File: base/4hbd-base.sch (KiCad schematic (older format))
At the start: 13 parts, among them J1 Screw_Terminal_01x03, J10 Screw_Terminal_01x04, J11 Screw_Terminal_01x02, J12 Conn_01x03, J13 Conn_01x08, J2 Screw_Terminal_01x03, J3 Screw_Terminal_01x03, J4 Screw_Terminal_01x03, J5 Screw_Terminal_01x02, J6 Screw_Terminal_01x02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

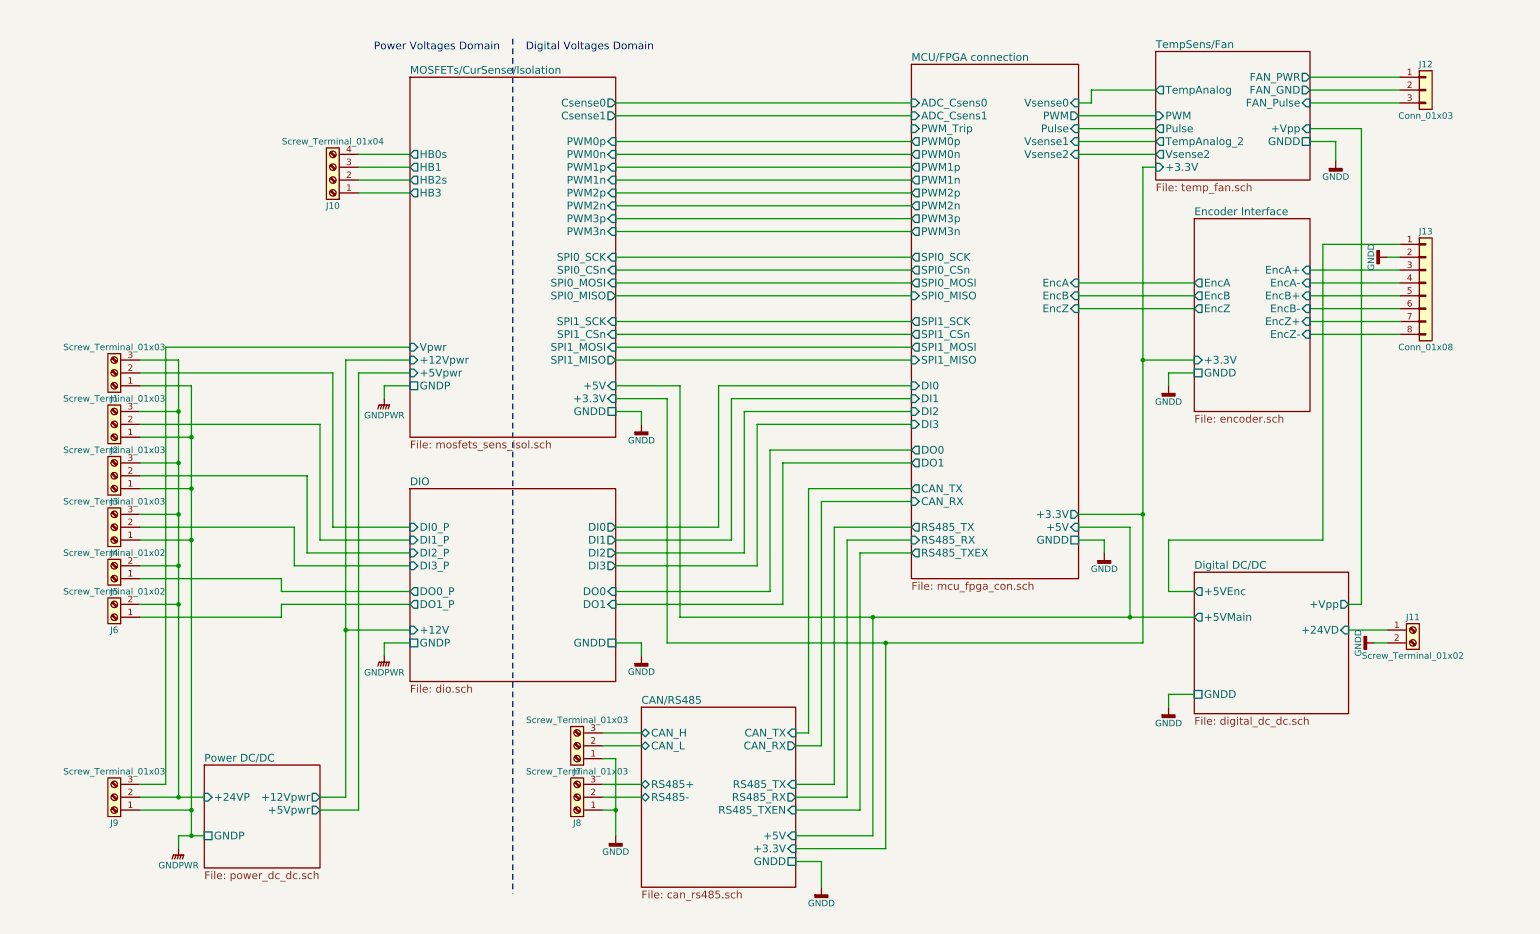
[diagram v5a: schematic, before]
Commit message: some test points
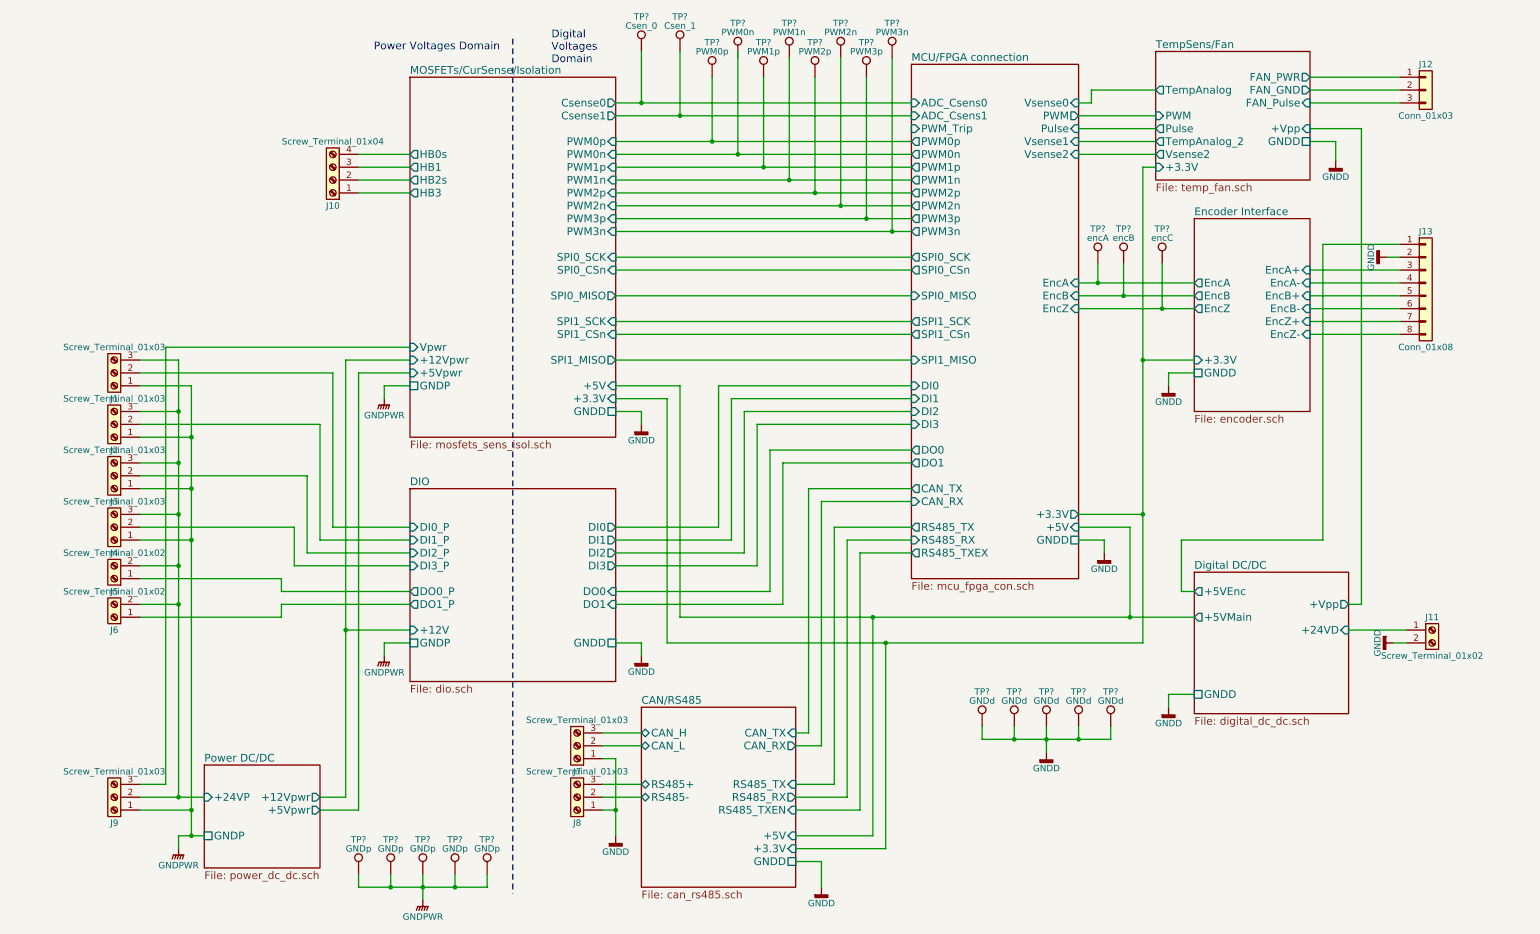
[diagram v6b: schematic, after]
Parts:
- added TP?: PWM0p, symbol Test_Point
- added TP?: PWM0n, symbol Test_Point
- added TP?: PWM1p, symbol Test_Point
- added TP?: PWM1n, symbol Test_Point
- added TP?: PWM2p, symbol Test_Point
- added TP?: PWM2n, symbol Test_Point
- added TP?: PWM3p, symbol Test_Point
- added TP?: PWM3n, symbol Test_Point
- added TP?: Csen_0, symbol Test_Point
- added TP?: Csen_1, symbol Test_Point
- added TP?: encA, symbol Test_Point
- added TP?: encB, symbol Test_Point
- added TP?: encC, symbol Test_Point
- added TP? (x5): GNDd, symbol Test_Point
- added TP? (x5): GNDp, symbol Test_Point
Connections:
- net Encoder Interface/EncA: now also TP?.1
- net Encoder Interface/EncB: now also TP?.1
- net Encoder Interface/EncZ: now also TP?.1
- net GNDD: now also TP?.1, TP?.1, TP?.1, TP?.1, TP?.1
- net GNDPWR: now also TP?.1, TP?.1, TP?.1, TP?.1, TP?.1
- net MCU/FPGA connection/ADC_Csens0: now also TP?.1
- net MCU/FPGA connection/ADC_Csens1: now also TP?.1
- net MCU/FPGA connection/PWM0p: now also TP?.1
- net MCU/FPGA connection/PWM1n: now also TP?.1
- net MCU/FPGA connection/PWM1p: now also TP?.1
- net MCU/FPGA connection/PWM2n: now also TP?.1
- net MCU/FPGA connection/PWM2p: now also TP?.1
- net MCU/FPGA connection/PWM3n: now also TP?.1
- net MCU/FPGA connection/PWM3p: now also TP?.1
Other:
- note added: "Digital \nVoltages\nDomain"
- note removed: "Digital Voltages Domain"
- moved on the sheet: J11

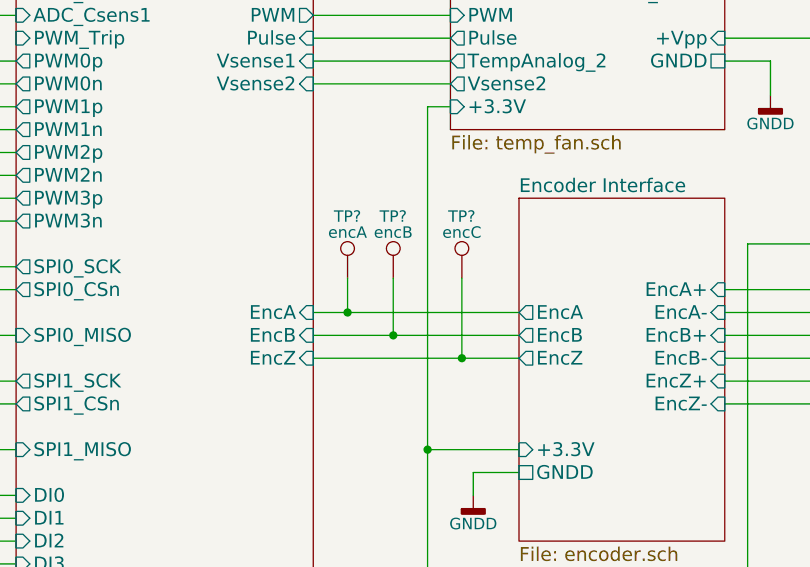
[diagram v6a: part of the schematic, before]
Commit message: A few updates to test points.
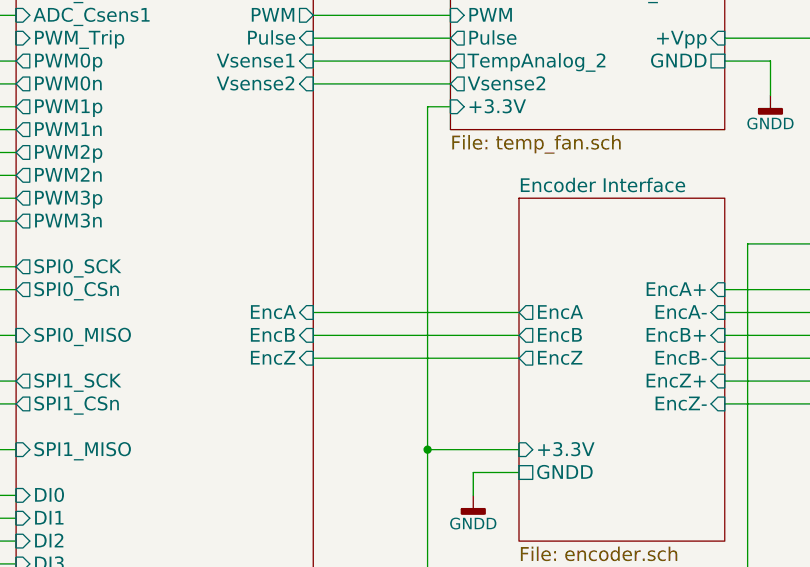
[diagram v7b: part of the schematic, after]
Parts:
- removed TP?: encA, symbol Test_Point
- removed TP?: encB, symbol Test_Point
- removed TP?: encC, symbol Test_Point
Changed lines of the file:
@@
 F14 "SPI0_SCK" I R 4600 2500 60
 F15 "SPI0_CSn" I R 4600 2600 60
-F17 "SPI0_MISO" O R 4600 2800 60
-F18 "SPI1_SCK" I R 4600 3000 60
-F19 "SPI1_CSn" I R 4600 3100 60
-F21 "SPI1_MISO" O R 4600 3300 60
-F22 "+3.3V" I R 4600 3600 60
-F23 "GNDD" U R 4600 3700 60
-F24 "Vpwr" I L 3000 3200 60
-F25 "+12Vpwr" I L 3000 3300 60
-F26 "GNDP" U L 3000 3500 60
-F27 "+5Vpwr" I L 3000 3400 60
-F28 "+5V" I R 4600 3500 60
-F29 "Csense0" O R 4600 1300 60
-F30 "Csense1" O R 4600 1400 60
+F16 "SPI0_MISO" O R 4600 2800 60
+F17 "SPI1_SCK" I R 4600 3000 60
+F18 "SPI1_CSn" I R 4600 3100 60
+F19 "SPI1_MISO" O R 4600 3300 60
+F20 "+3.3V" I R 4600 3600 60
+F21 "GNDD" U R 4600 3700 60
+F22 "Vpwr" I L 3000 3200 60
+F23 "+12Vpwr" I L 3000 3300 60
+F24 "GNDP" U L 3000 3500 60
+F25 "+5Vpwr" I L 3000 3400 60
+F26 "+5V" I R 4600 3500 60
+F27 "Csense0" O R 4600 1300 60
+F28 "Csense1" O R 4600 1400 60
 $EndSheet
 $Sheet
@@
 F10 "SPI0_SCK" O L 6900 2500 60
 F11 "SPI0_CSn" O L 6900 2600 60
-F13 "SPI0_MISO" I L 6900 2800 60
-F14 "SPI1_SCK" O L 6900 3000 60
-F15 "SPI1_CSn" O L 6900 3100 60
-F17 "SPI1_MISO" I L 6900 3300 60
-F18 "DI0" I L 6900 3500 60
-F19 "DI1" I L 6900 3600 60
-F20 "DI2" I L 6900 3700 60
-F21 "DI3" I L 6900 3800 60
-F22 "DO0" O L 6900 4000 60
-F23 "DO1" O L 6900 4100 60
-F24 "CAN_TX" O L 6900 4300 60
-F25 "CAN_RX" I L 6900 4400 60
-F26 "RS485_TX" O L 6900 4600 60
-F27 "RS485_RX" I L 6900 4700 60
-F28 "RS485_TXEX" O L 6900 4800 60
-F29 "+5V" I R 8200 4600 60
-F30 "GNDD" U R 8200 4700 60
-F31 "EncA" I R 8200 2700 60
-F32 "EncB" I R 8200 2800 60
-F33 "EncZ" I R 8200 2900 60
-F34 "PWM" O R 8200 1400 60
-F35 "Pulse" I R 8200 1500 60
-F36 "Vsense1" I R 8200 1600 60
-F37 "+3.3V" O R 8200 4500 60
-F38 "PWM_Trip" I L 6900 1500 60
-F39 "Vsense0" I R 8200 1300 60
-F40 "ADC_Csens1" I L 6900 1400 60
-F41 "ADC_Csens0" I L 6900 1300 60
-F42 "Vsense2" I R 8200 1700 60
+F12 "SPI0_MISO" I L 6900 2800 60
+F13 "SPI1_SCK" O L 6900 3000 60
+F14 "SPI1_CSn" O L 6900 3100 60
+F15 "SPI1_MISO" I L 6900 3300 60
+F16 "DI0" I L 6900 3500 60
+F17 "DI1" I L 6900 3600 60
+F18 "DI2" I L 6900 3700 60
+F19 "DI3" I L 6900 3800 60
+F20 "DO0" O L 6900 4000 60
+F21 "DO1" O L 6900 4100 60
+F22 "CAN_TX" O L 6900 4300 60
+F23 "CAN_RX" I L 6900 4400 60
+F24 "RS485_TX" O L 6900 4600 60
+F25 "RS485_RX" I L 6900 4700 60
+F26 "RS485_TXEX" O L 6900 4800 60
+F27 "+5V" I R 8200 4600 60
+F28 "GNDD" U R 8200 4700 60
+F29 "EncA" I R 8200 2700 60
+F30 "EncB" I R 8200 2800 60
+F31 "EncZ" I R 8200 2900 60
+F32 "PWM" O R 8200 1400 60
+F33 "Pulse" I R 8200 1500 60
+F34 "Vsense1" I R 8200 1600 60
+F35 "+3.3V" O R 8200 4500 60
+F36 "PWM_Trip" I L 6900 1500 60
+F37 "Vsense0" I R 8200 1300 60
+F38 "ADC_Csens1" I L 6900 1400 60
+F39 "ADC_Csens0" I L 6900 1300 60
+F40 "Vsense2" I R 8200 1700 60
 $EndSheet
 $Sheet
@@
 Connection ~ 5100 1400
 $Comp
-L Test_Point TP?
-U 1 1 5A478D44
-P 8350 2550
-F 0 "TP?" H 8350 2820 50  0000 C CNN
-F 1 "encA" H 8350 2750 50  0000 C CNN
-F 2 "" H 8550 2550 50  0001 C CNN
-F 3 "" H 8550 2550 50  0001 C CNN
-	1    8350 2550
-	1    0    0    -1
-$EndComp
-$Comp
-L Test_Point TP?
-U 1 1 5A479C9D
-P 8550 2550
-F 0 "TP?" H 8550 2820 50  0000 C CNN
-F 1 "encB" H 8550 2750 50  0000 C CNN
-F 2 "" H 8750 2550 50  0001 C CNN
-F 3 "" H 8750 2550 50  0001 C CNN
-	1    8550 2550
-	1    0    0    -1
-$EndComp
-$Comp
-L Test_Point TP?
-U 1 1 5A47A006
-P 8850 2550
-F 0 "TP?" H 8850 2820 50  0000 C CNN
-F 1 "encC" H 8850 2750 50  0000 C CNN
-F 2 "" H 9050 2550 50  0001 C CNN
-F 3 "" H 9050 2550 50  0001 C CNN
-	1    8850 2550
-	1    0    0    -1
-$EndComp
-Wire Wire Line
-	8350 2550 8350 2700
-Connection ~ 8350 2700
-Wire Wire Line
-	8550 2550 8550 2800
-Connection ~ 8550 2800
-Wire Wire Line
-	8850 2550 8850 2900
-Connection ~ 8850 2900
-$Comp
 L GNDD #PWR?

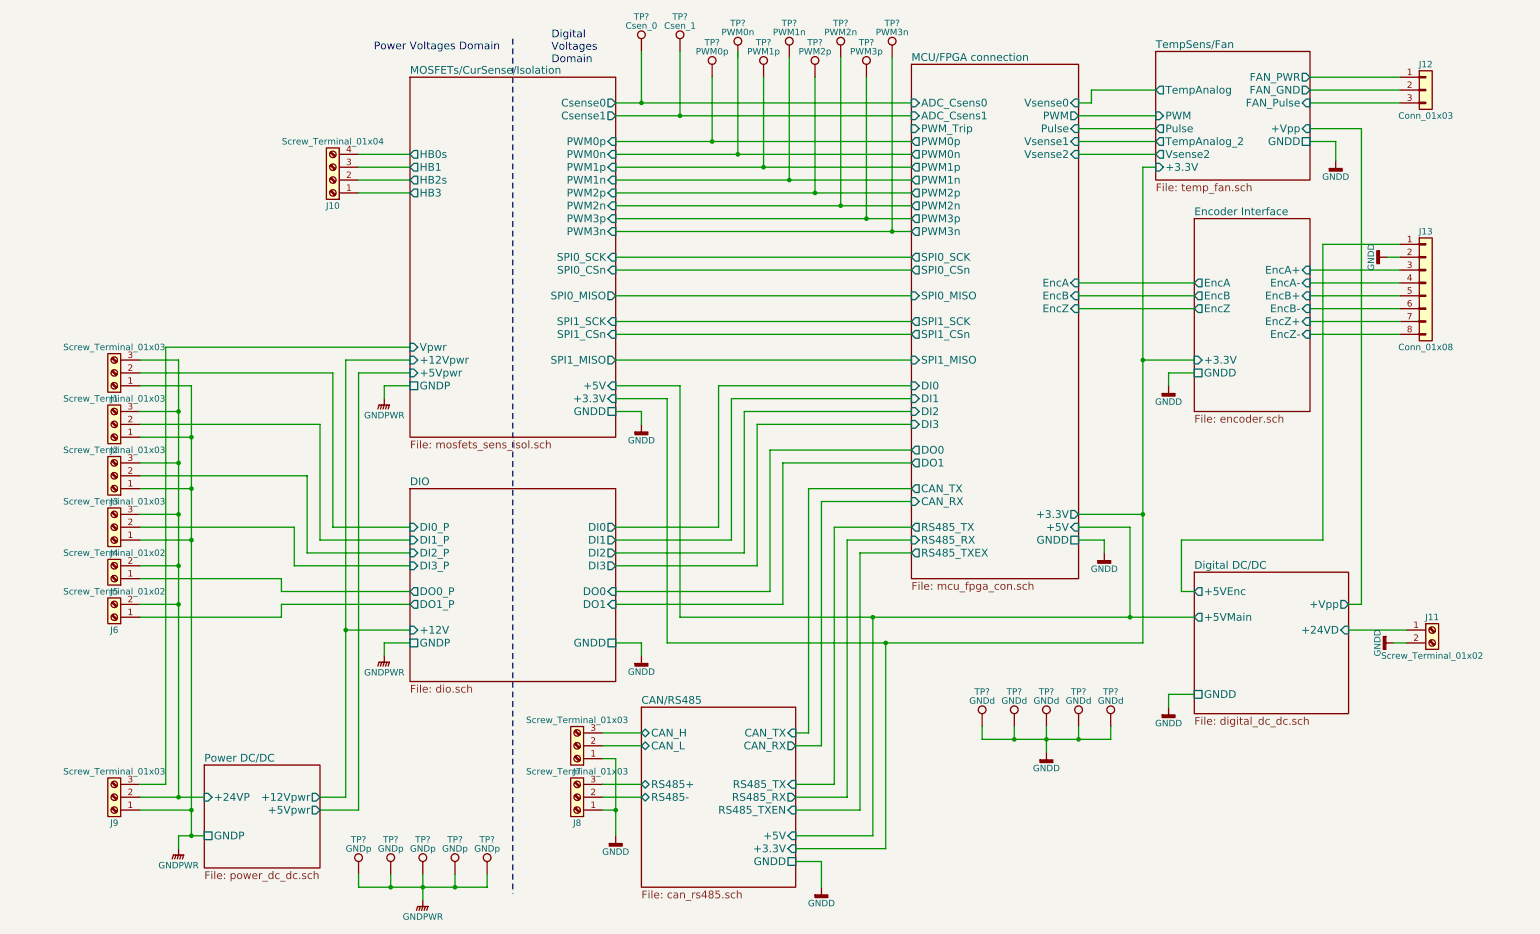
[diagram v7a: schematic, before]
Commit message: update to spring terminal 2.54 KF141R
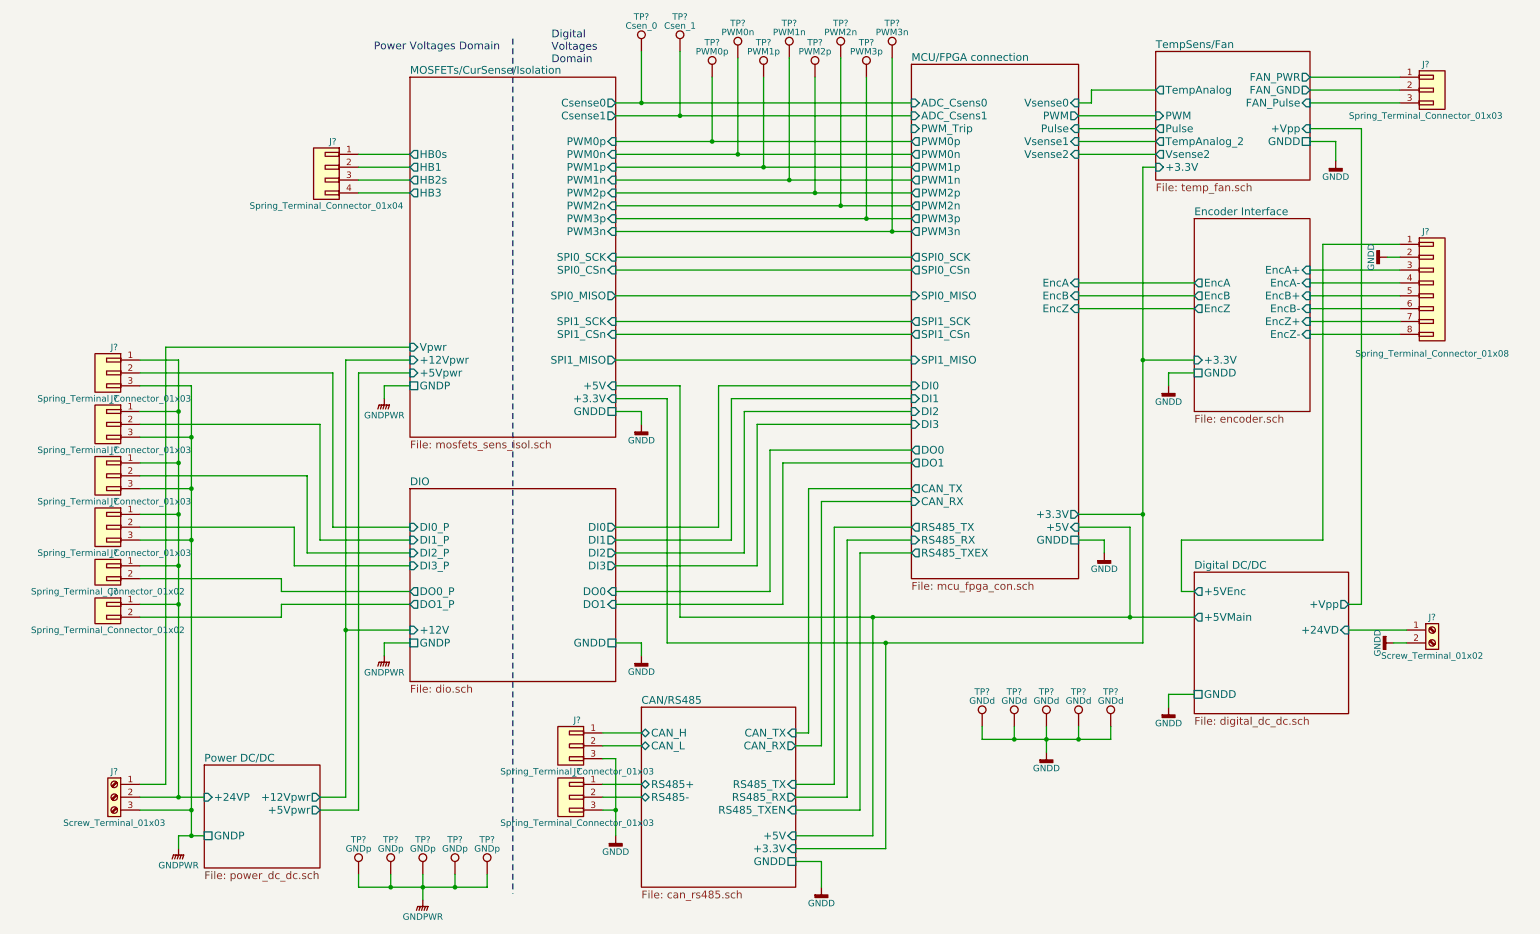
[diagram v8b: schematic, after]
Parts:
- removed J1, J2, J3, J4, J7, J8, J9: Screw_Terminal_01x03, symbol Screw_Terminal_01x03
- removed J10: Screw_Terminal_01x04, symbol Screw_Terminal_01x04
- removed J11, J5, J6: Screw_Terminal_01x02, symbol Screw_Terminal_01x02
- removed J12: Conn_01x03, symbol Conn_01x03
- removed J13: Conn_01x08, Connector_PinHeader_2.54mm:PinHeader_1x08_P2.54mm_Horizontal, symbol Conn_01x08
- added J? (x7): Spring_Terminal_Connector_01x03, TerminalBlock:SpringTerminalBlock_KF141R_3_P2.54mm, symbol Spring_Terminal_Connector_01x03
- added J?: Screw_Terminal_01x03, TerminalBlock:TerminalBlock_Altech_AK300-3_P5.00mm, symbol Screw_Terminal_01x03
- added J?: Spring_Terminal_Connector_01x04, symbol Spring_Terminal_Connector_01x04
- added J?: Screw_Terminal_01x02, TerminalBlock:TerminalBlock_Altech_AK300-2_P5.00mm, symbol Screw_Terminal_01x02
- added J?: Spring_Terminal_Connector_01x08, TerminalBlock:SpringTerminalBlock_KF141R_8_P2.54mm, symbol Spring_Terminal_Connector_01x08
- added J? (x2): Spring_Terminal_Connector_01x02, TerminalBlock:SpringTerminalBlock_KF141R_2_P2.54mm, symbol Spring_Terminal_Connector_01x02
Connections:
- net CAN/RS485/CAN_H: now also J?.1 (Pin_1)
- net CAN/RS485/CAN_L: now also J?.2 (Pin_2)
- net CAN/RS485/RS485+: now also J?.1 (Pin_1)
- net CAN/RS485/RS485-: now also J?.2 (Pin_2)
- net DIO/DI0_P: now also J?.2 (Pin_2)
- net DIO/DI1_P: now also J?.2 (Pin_2)
- net DIO/DI2_P: now also J?.2 (Pin_2)
- net DIO/DI3_P: now also J?.2 (Pin_2)
- net DIO/DO0_P: now also J?.2 (Pin_2)
- net DIO/DO1_P: now also J?.2 (Pin_2)
- net Digital DC/DC/+24VD: now also J?.1 (Pin_1)
- net Digital DC/DC/+5VEnc: now also J?.1 (Pin_1)
- net Encoder Interface/EncA+: now also J?.3 (Pin_3)
- net Encoder Interface/EncA-: now also J?.4 (Pin_4)
- net Encoder Interface/EncB+: now also J?.5 (Pin_5)
- net Encoder Interface/EncB-: now also J?.6 (Pin_6)
- net Encoder Interface/EncZ+: now also J?.7 (Pin_7)
- net Encoder Interface/EncZ-: now also J?.8 (Pin_8)
- net GNDD: now also J?.2 (Pin_2), J?.2 (Pin_2), J?.3 (Pin_3), J?.3 (Pin_3)
- net GNDPWR: now also J?.3 (Pin_3), J?.3 (Pin_3), J?.3 (Pin_3), J?.3 (Pin_3), J?.3 (Pin_3)
- net MCU/FPGA connection/PWM0n: now also TP?.1
- net MOSFETs/CurSense/Isolation/HB0s: now also J?.1 (Pin_1)
- net MOSFETs/CurSense/Isolation/HB1: now also J?.2 (Pin_2)
- net MOSFETs/CurSense/Isolation/HB2s: now also J?.3 (Pin_3)
- net MOSFETs/CurSense/Isolation/HB3: now also J?.4 (Pin_4)
- net MOSFETs/CurSense/Isolation/Vpwr: now also J?.1 (Pin_1)
- net Power DC/DC/+24VP: now also J?.1 (Pin_1), J?.1 (Pin_1), J?.1 (Pin_1), J?.1 (Pin_1), J?.1 (Pin_1), J?.1 (Pin_1), J?.2 (Pin_2)
- net TempSens/Fan/FAN_GND: now also J?.2 (Pin_2)
- net TempSens/Fan/FAN_PWR: now also J?.1 (Pin_1)
- net TempSens/Fan/FAN_Pulse: now also J?.3 (Pin_3)
